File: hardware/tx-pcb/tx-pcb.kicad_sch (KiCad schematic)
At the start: 32 parts, among them J1 SWD_Pins, J2 CC1101_RF_Module_Conn, J3 USB2.0_C_16P, J4 Conn_Coaxial_Small, SW1 SW_Push, U1 STM32WB55CEUx, U2 USBLC6-2SC6, X1 NX2016SA-32MHZ-STD-CZS-5

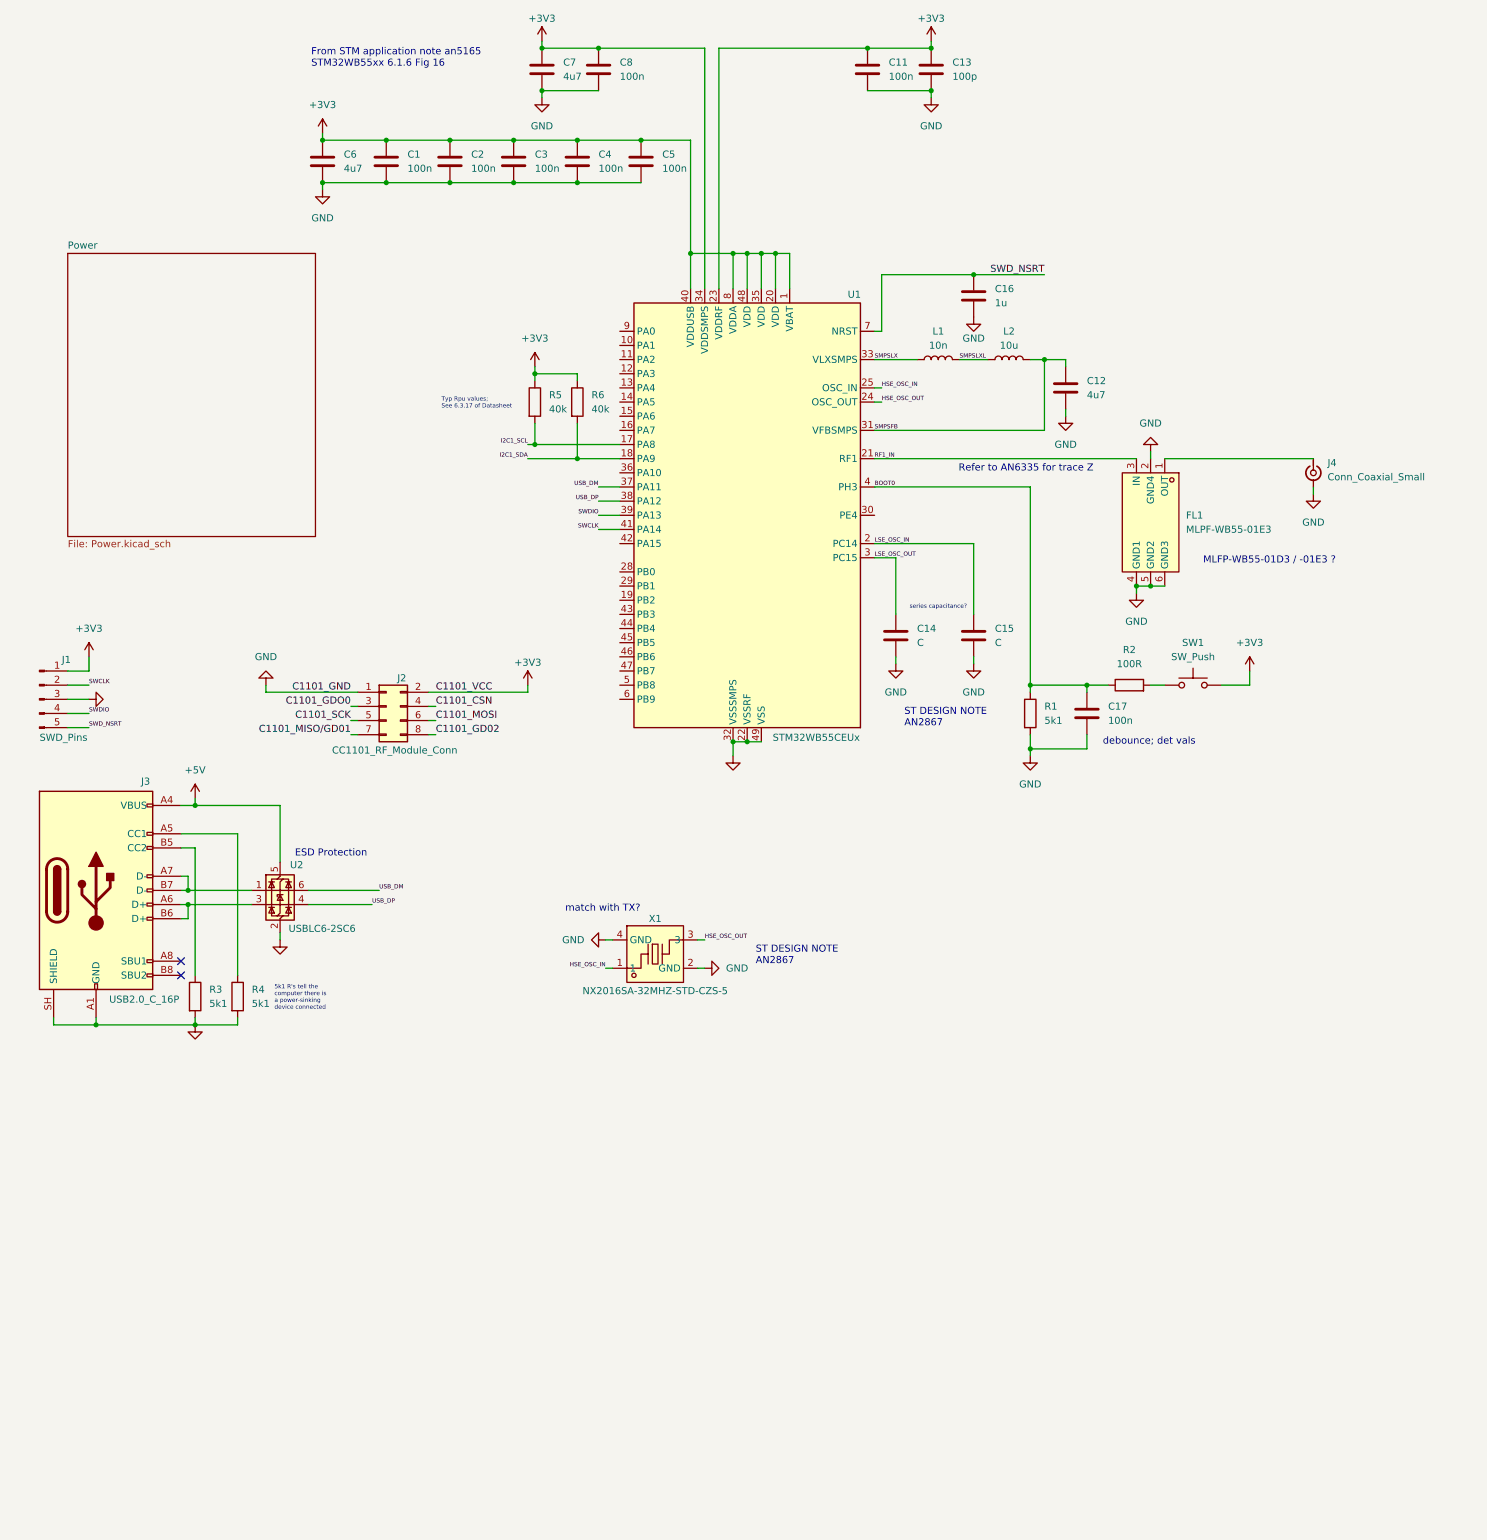
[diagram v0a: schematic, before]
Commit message: sx1262 TXRX board, follows Semtech's own dev board schematic
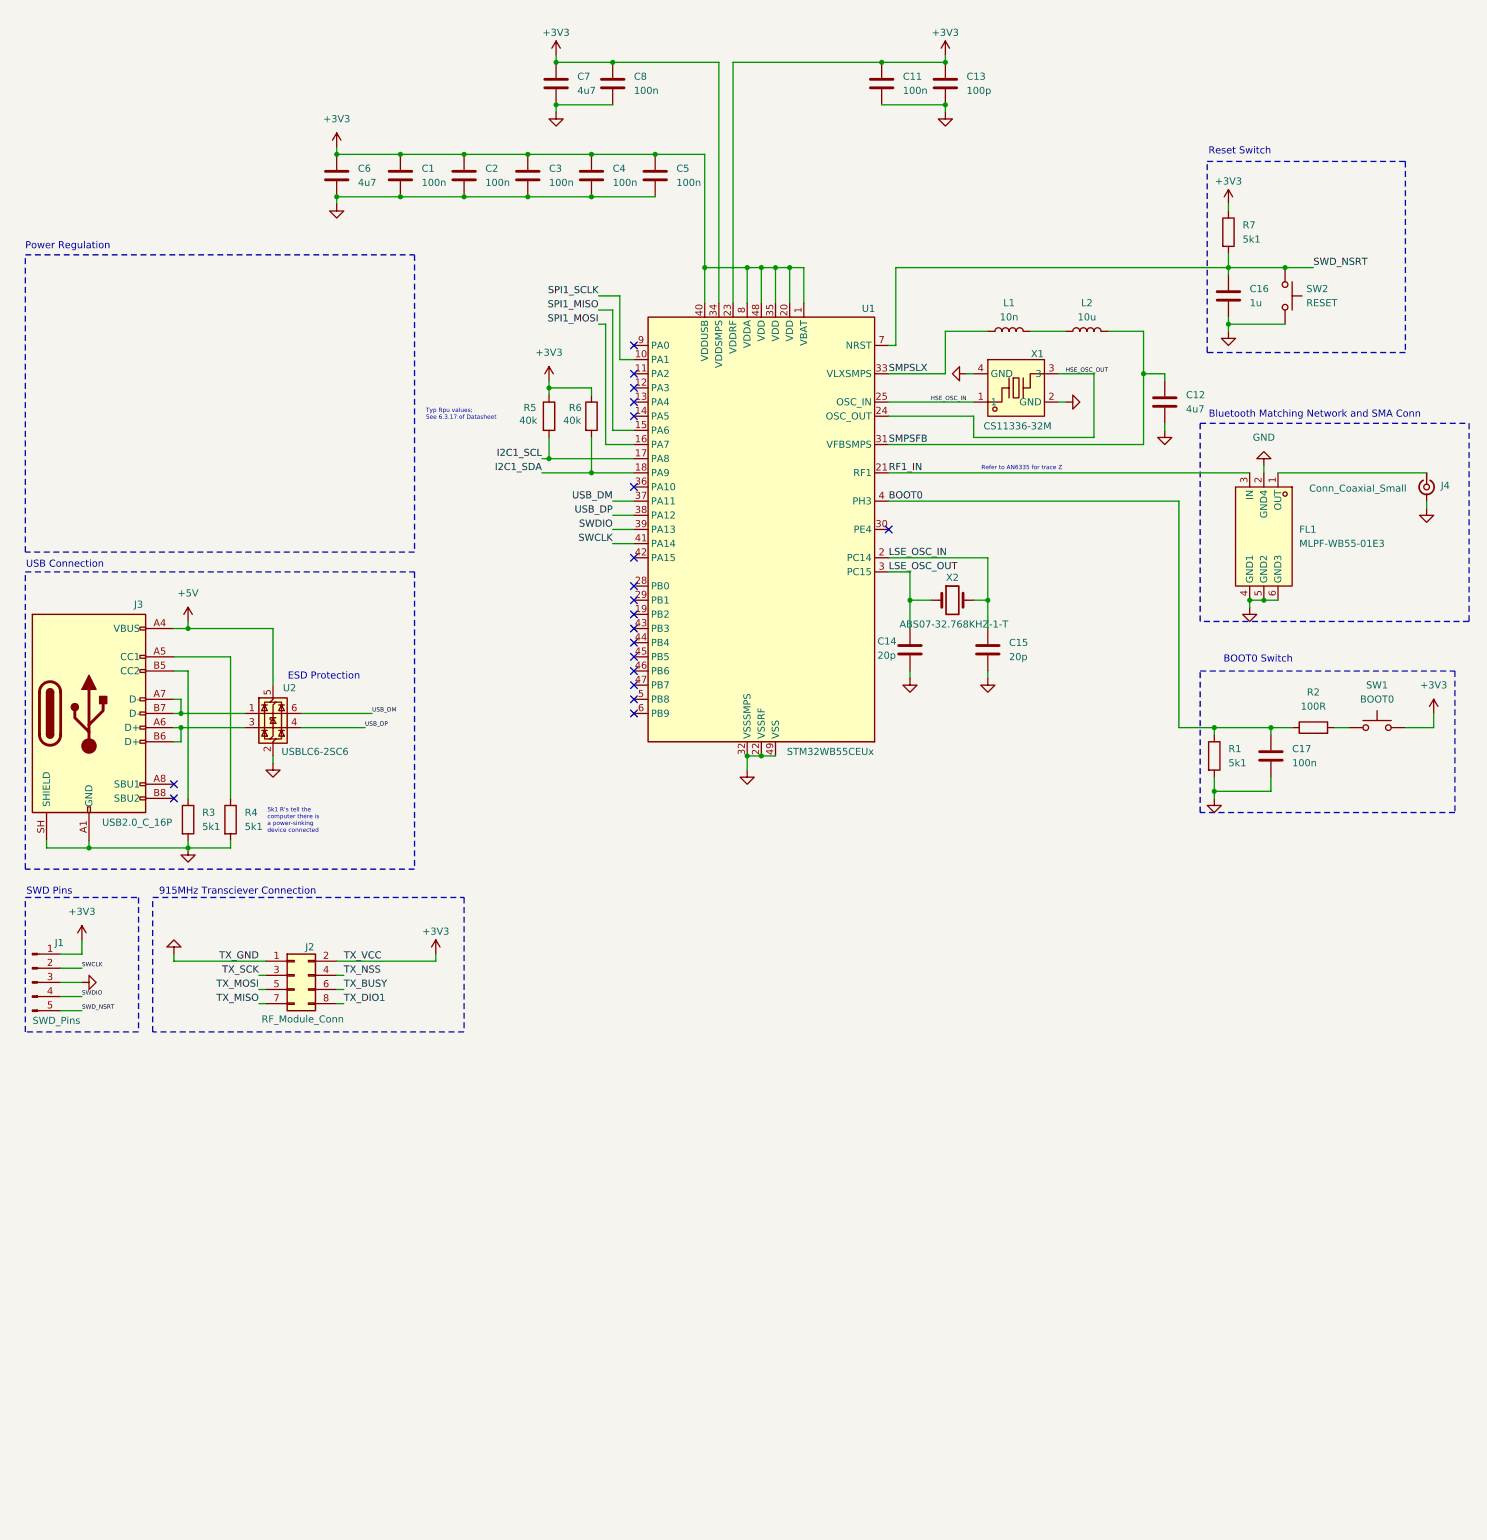
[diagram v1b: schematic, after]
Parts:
- removed X1: NX2016SA-32MHZ-STD-CZS-5, easyeda2kicad:OSC-SMD_4P-L2.0-W1.6-BL, symbol easyeda2kicad:NX2016SA-32MHZ-STD-CZS-5
- added R7: 5k1, symbol Device:R
- added SW2: RESET, Button_Switch_THT:SW_PUSH_6mm, symbol Switch:SW_Push
- added X1: CS11336-32M, EasyEDA:NX2016SA_NDK, symbol rx-parts:Q22FA12800025
- added X2: ABS07-32.768KHZ-1-T, EasyEDA:OSC-SMD_2P-L3.2-W1.5, symbol Device:Crystal
- C14, C15: value C -> 20p
- J2: value CC1101_RF_Module_Conn -> RF_Module_Conn; footprint (none) -> Connector_PinHeader_2.00mm:PinHeader_2x04_P2.00mm_Vertical
- SW1: value SW_Push -> BOOT0; footprint (none) -> Button_Switch_THT:SW_PUSH_6mm
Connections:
- net +3V3: now also R7.1
- net GND: now also SW2.2, X1.2 (GND), X1.4 (GND)
- net HSE_OSC_IN: now also X1.1
- net HSE_OSC_OUT: now also X1.3
- net LSE_OSC_IN: now also X2.2
- net LSE_OSC_OUT: now also X2.1
- net SWD_NSRT: now also R7.2, SW2.1
- net SPI1_SCLK: now reaches U1.10 (PA1)
- net SPI1_MISO: now reaches U1.15 (PA6)
- net SPI1_MOSI: now reaches U1.16 (PA7)
- net C1101_CSN renamed TX_NSS
- net C1101_GD02 renamed TX_DIO1
- net C1101_GDO0 renamed TX_SCK
- net C1101_MISO/GD01 renamed TX_MISO
- net C1101_MOSI renamed TX_BUSY
- net C1101_SCK renamed TX_MOSI
- net SMPSLXL: no longer names the net of L1.2, L2.1
- no-connect marks 2 -> 20
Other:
- removed sheet Power
- note added: "915MHz Transciever Connection"
- note added: "BOOT0 Switch"
- note added: "Bluetooth Matching Network and SMA Conn"
- note added: "Power Regulation"
- note added: "Reset Switch"
- note added: "SWD Pins"
- note added: "USB Connection"
- note removed: "From STM application note an5165 STM32WB55xx 6.1.6 Fig 16"
- note removed: "MLFP-WB55-01D3 / -01E3 ?"
- note removed: "ST DESIGN NOTE AN2867"
- note removed: "debounce; det vals"
- note removed: "match with TX?"
- note removed: "series capacitance?"

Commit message: minor updates
updated footprints, added some indicator LEDs, created a project library so we dont need to match easyeda libraries
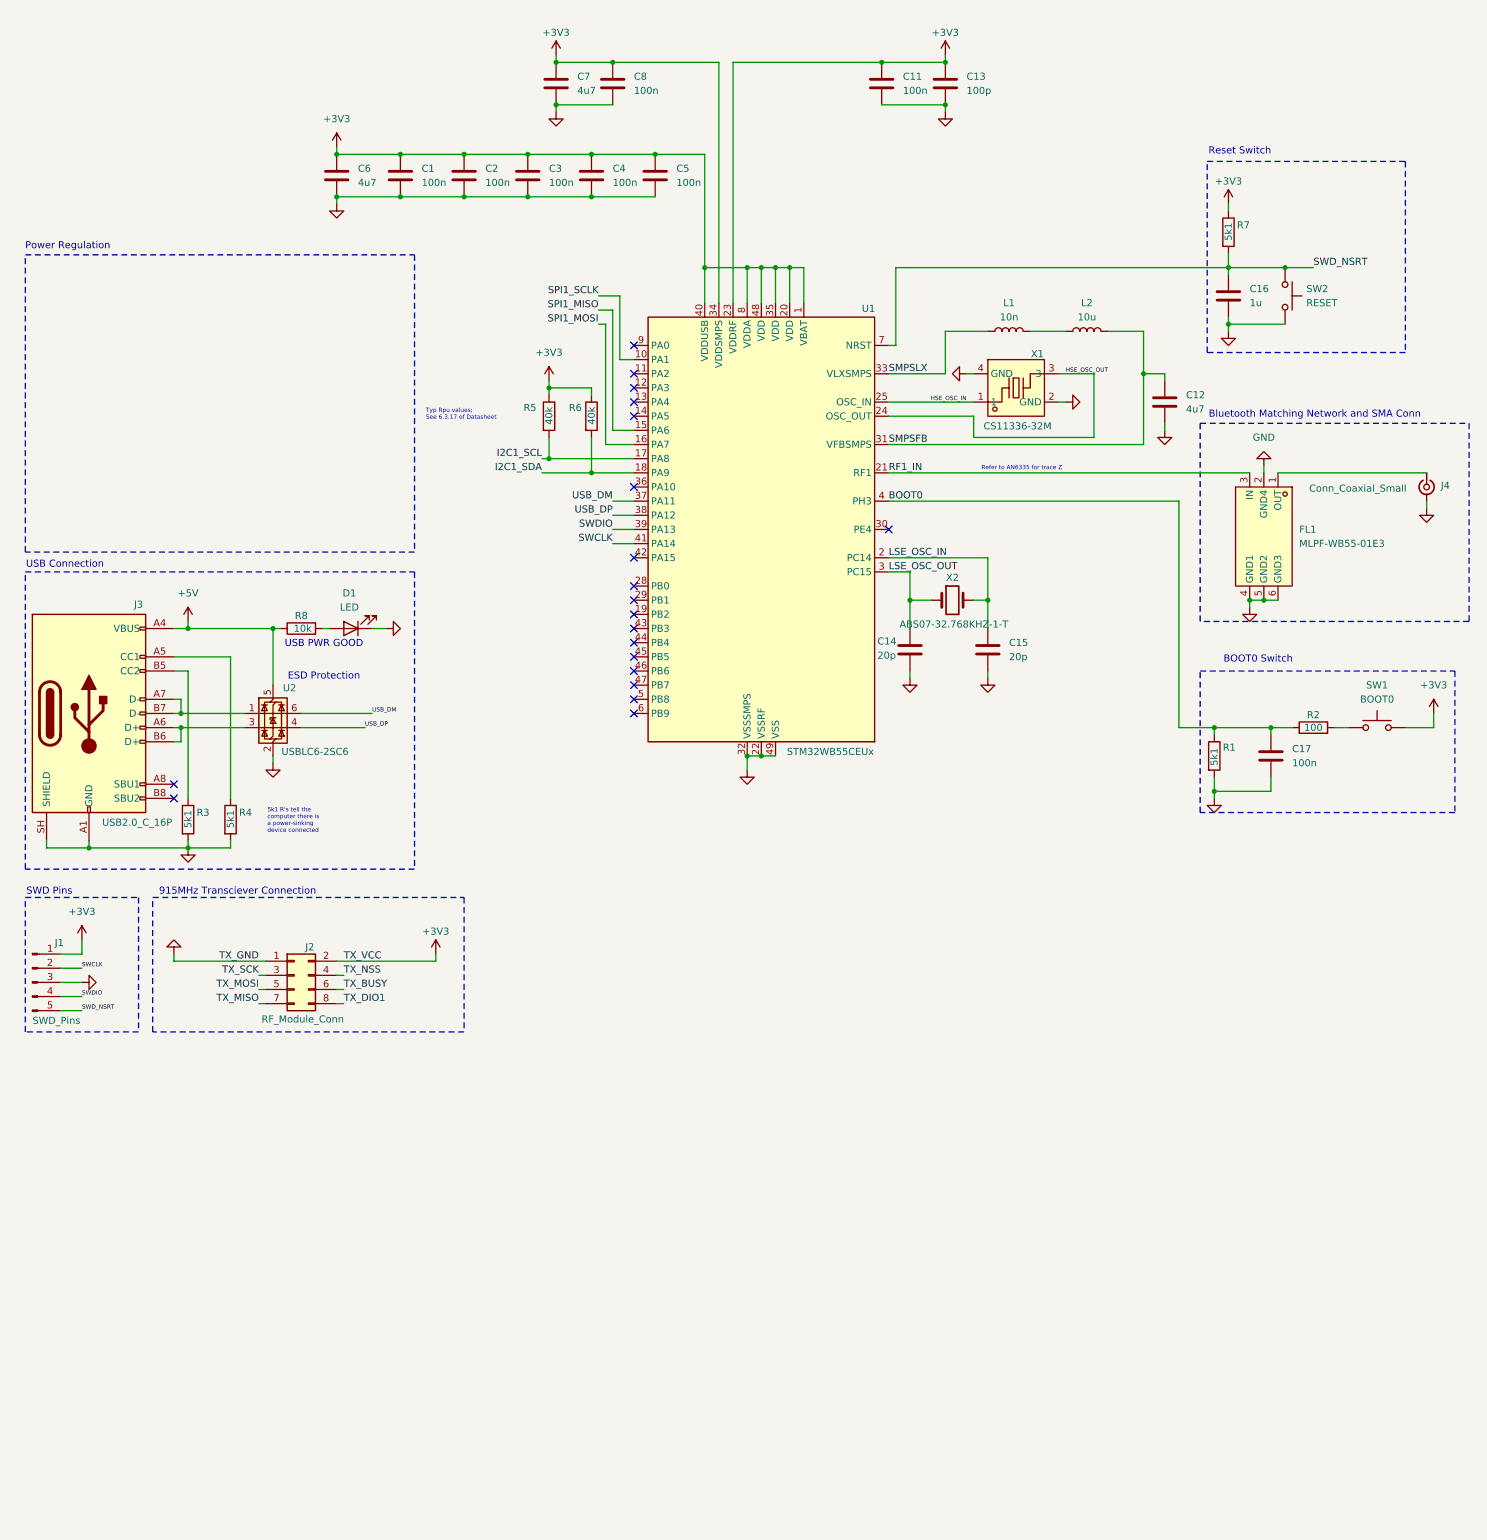
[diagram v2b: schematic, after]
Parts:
- added D1: LED, LED_SMD:LED_0603_1608Metric_Pad1.05x0.95mm_HandSolder, symbol Device:LED
- added R8: 10k, Resistor_SMD:R_0805_2012Metric_Pad1.20x1.40mm_HandSolder, symbol Device:R
- C1, C11, C12, C13, C14, C15, C16, C17, C2, C3, C4, C5, C6, C7, C8: footprint (none) -> Capacitor_SMD:C_0603_1608Metric_Pad1.08x0.95mm_HandSolder
- J1: footprint (none) -> Connector_PinSocket_2.54mm:PinSocket_1x05_P2.54mm_Vertical
- J3: footprint (none) -> rf-pwr-tx-library:USB-C-SMD_GT-USB-7047A
- J4: footprint (none) -> Connector_Coaxial:SMA_BAT_Wireless_BWSMA-KWE-Z001
- L1, L2: footprint (none) -> Inductor_SMD:L_0805_2012Metric_Pad1.05x1.20mm_HandSolder
- R1, R3, R4, R5, R6, R7: footprint (none) -> Resistor_SMD:R_0805_2012Metric_Pad1.20x1.40mm_HandSolder
- R2: value 100R -> 100; footprint (none) -> Resistor_SMD:R_0805_2012Metric_Pad1.20x1.40mm_HandSolder
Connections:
- net +5V: now also R8.1
- net GND: now also D1.1 (K)
- new net: D1.2 (A), R8.2
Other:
- note added: "USB PWR GOOD"

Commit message: updated footprint library
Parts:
- FL1: footprint easyeda2kicad:FILTER-SMD_6P-L1.6-W1.0-P0.50-BL -> rf-pwr-tx-library:FILTER-SMD_6P-L1.6-W1.0-P0.50-BL
- X1: footprint EasyEDA:NX2016SA_NDK -> rf-pwr-tx-library:NX2016SA_NDK
- X2: footprint EasyEDA:OSC-SMD_2P-L3.2-W1.5 -> rf-pwr-tx-library:OSC-SMD_2P-L3.2-W1.5
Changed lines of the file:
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@@
 			)
 		)
-		(property "Footprint" "EasyEDA:NX2016SA_NDK"
+		(property "Footprint" "rf-pwr-tx-library:NX2016SA_NDK"
 			(at 193.04 90.17 0)
 			(hide yes)
@@
 			)
 		)
-		(property "Footprint" "easyeda2kicad:FILTER-SMD_6P-L1.6-W1.0-P0.50-BL"
+		(property "Footprint" "rf-pwr-tx-library:FILTER-SMD_6P-L1.6-W1.0-P0.50-BL"
 			(at 227.33 106.68 0)
 			(hide yes)
@@
 			)
 		)
-		(property "Footprint" "EasyEDA:OSC-SMD_2P-L3.2-W1.5"
+		(property "Footprint" "rf-pwr-tx-library:OSC-SMD_2P-L3.2-W1.5"
 			(at 181.61 118.11 0)
 			(hide yes)
